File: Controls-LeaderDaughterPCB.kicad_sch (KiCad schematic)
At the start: 23 parts, among them U8 LMC555xM

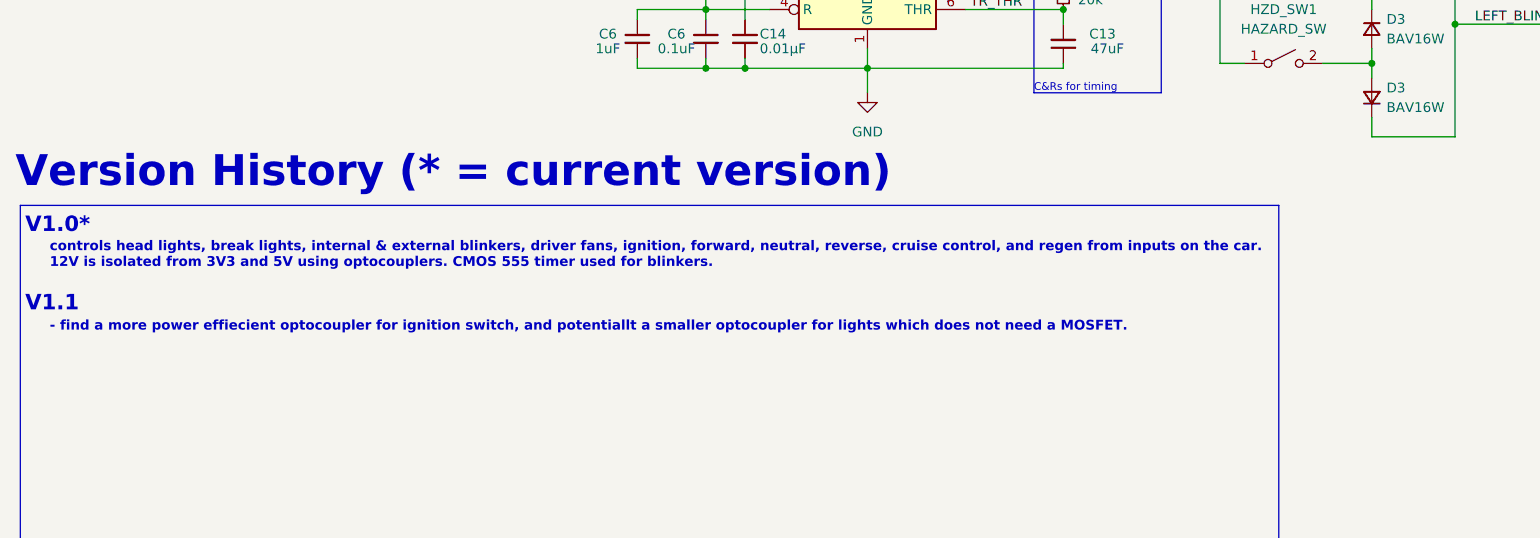
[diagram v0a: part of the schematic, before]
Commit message: lower power optocouplers now used for lights and fans, updated version history
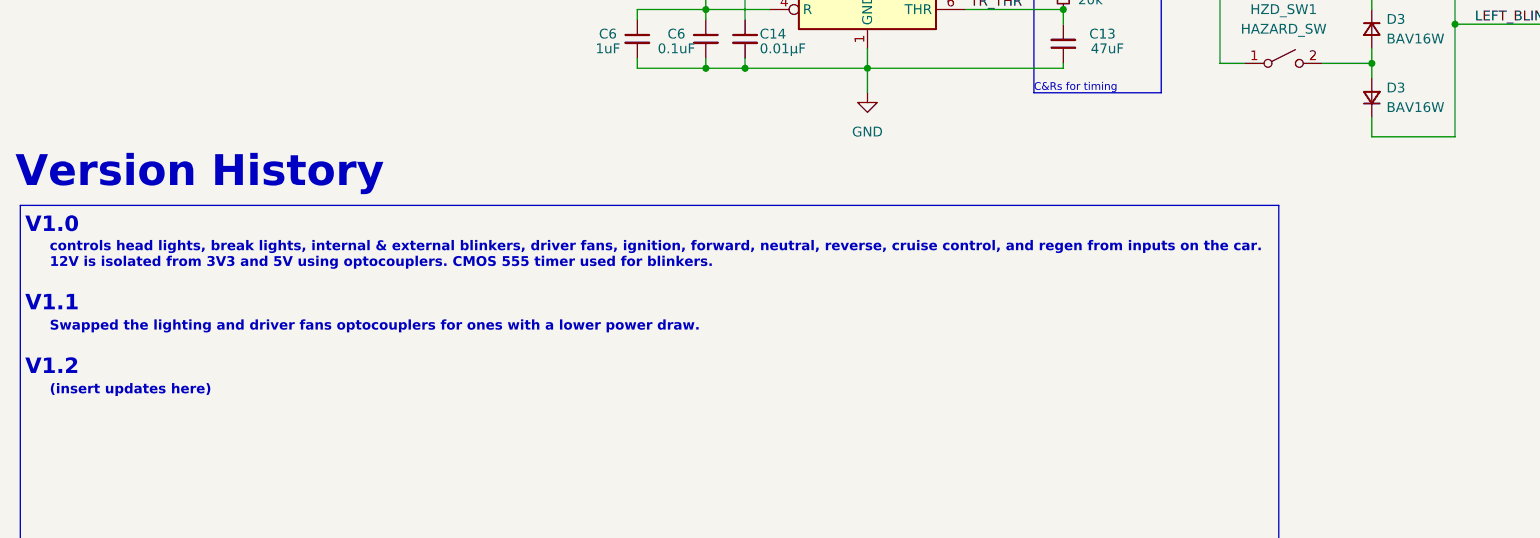
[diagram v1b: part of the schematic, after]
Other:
- note added: "(insert updates here)"
- note added: "Swapped the lighting and driver fans optocouplers for ones with a lower power draw."
- note added: "V1.0"
- note added: "V1.2"
- note added: "Version History"
- note removed: "- find a more power effiecient optocoupler for ignition switch, and potentiallt a smaller optocoupler for lights which does not need a MOSFET."
- note removed: "V1.0*"
- note removed: "Version History (* = current version)"

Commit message: changed version history
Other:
- note added: "Controls head lights, break lights, internal & external blinkers, driver fans, ignition, forward, neutral, reverse, cruise control, and regen from inputs on the car. 12V is isolated from 3V3 and 5V using optocouplers. CMOS 555 timer used for blinkers. See ReadME for more details."
- note removed: "controls head lights, break lights, internal & external blinkers, driver fans, ignition, forward, neutral, reverse, cruise control, and regen from inputs on the car. 12V is isolated from 3V3 and 5V using optocouplers. CMOS 555 timer used for blinkers."
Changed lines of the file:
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@@
     (effects (font (size 5 5) (thickness 0.7) bold) (justify left bottom))
   )
-  (text "controls head lights, break lights, internal & external blinkers, driver fans, ignition, forward, neutral, reverse, cruise control, and regen from inputs on the car.\n12V is isolated from 3V3 and 5V using optocouplers. CMOS 555 timer used for blinkers."
+  (text "Controls head lights, break lights, internal & external blinkers, driver fans, ignition, forward, neutral, reverse, cruise control, and regen from inputs on the car.\n12V is isolated from 3V3 and 5V using optocouplers. CMOS 555 timer used for blinkers. See ReadME for more details."
     (at 16.51 137.16 0)
     (effects (font (size 1.27 1.27) bold) (justify left bottom))

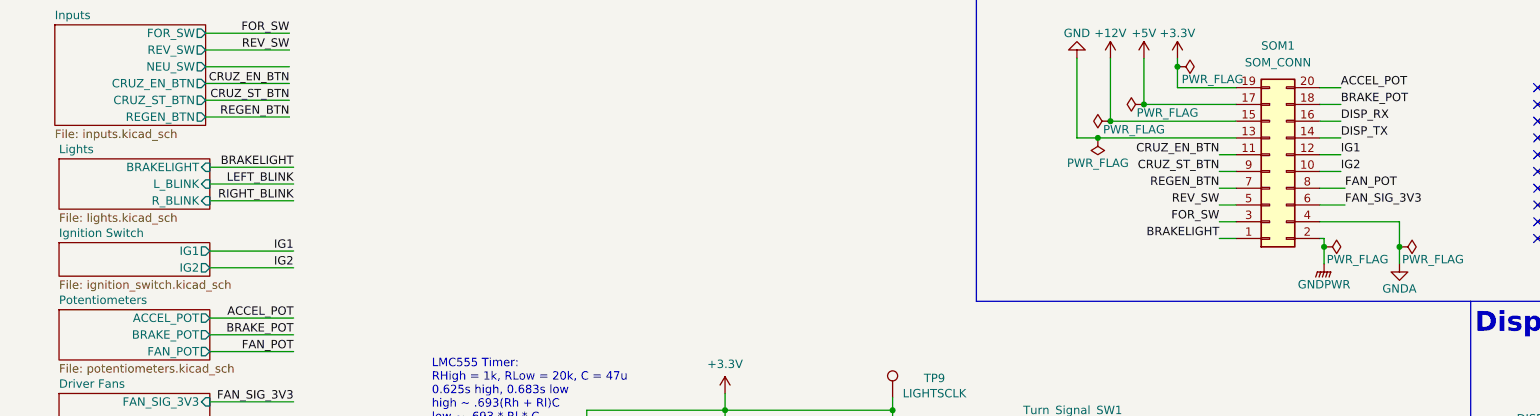
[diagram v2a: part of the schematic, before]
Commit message: Removed ignition switch connection and redid ignition signals
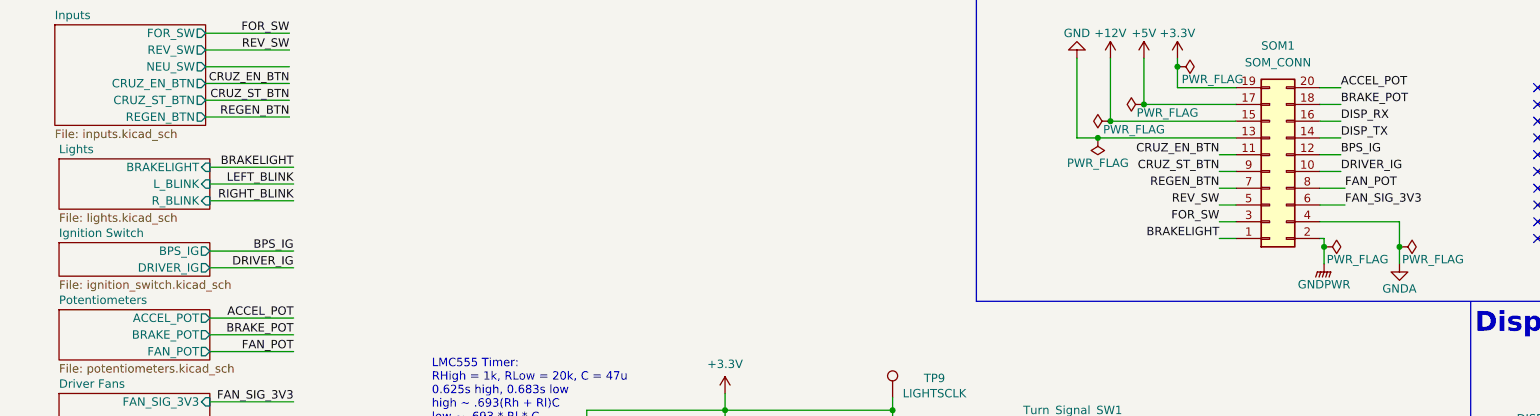
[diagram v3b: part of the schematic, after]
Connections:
- net IG1 renamed BPS_IG
- net IG2 renamed DRIVER_IG
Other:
- sheet Ignition Switch ports: added BPS_IG, DRIVER_IG; removed IG1, IG2
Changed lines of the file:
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@@
     (effects (font (size 1.27 1.27)) (justify right bottom))
   )
-  (label "IG2" (at 57.15 60.96 180) (fields_autoplaced)
+  (label "DRIVER_IG" (at 57.15 60.96 180) (fields_autoplaced)
     (effects (font (size 1.27 1.27)) (justify right bottom))
   )
@@
     (effects (font (size 1.27 1.27)) (justify right bottom))
   )
-  (label "IG2" (at 215.9 46.355 0) (fields_autoplaced)
+  (label "DRIVER_IG" (at 215.9 46.355 0) (fields_autoplaced)
     (effects (font (size 1.27 1.27)) (justify left bottom))
   )
@@
     (effects (font (size 1.27 1.27)) (justify right bottom))
   )
-  (label "IG1" (at 215.9 43.815 0) (fields_autoplaced)
+  (label "BPS_IG" (at 215.9 43.815 0) (fields_autoplaced)
     (effects (font (size 1.27 1.27)) (justify left bottom))
   )
-  (label "IG1" (at 57.15 58.42 180) (fields_autoplaced)
+  (label "BPS_IG" (at 57.15 58.42 180) (fields_autoplaced)
     (effects (font (size 1.27 1.27)) (justify right bottom))
   )
@@
       (effects (font (size 1.27 1.27)) (justify left top))
     )
-    (pin "IG1" output (at 44.45 58.42 0)
+    (pin "BPS_IG" output (at 44.45 58.42 0)
       (effects (font (size 1.27 1.27)) (justify right))
     )
-    (pin "IG2" output (at 44.45 60.96 0)
+    (pin "DRIVER_IG" output (at 44.45 60.96 0)
       (effects (font (size 1.27 1.27)) (justify right))
     )

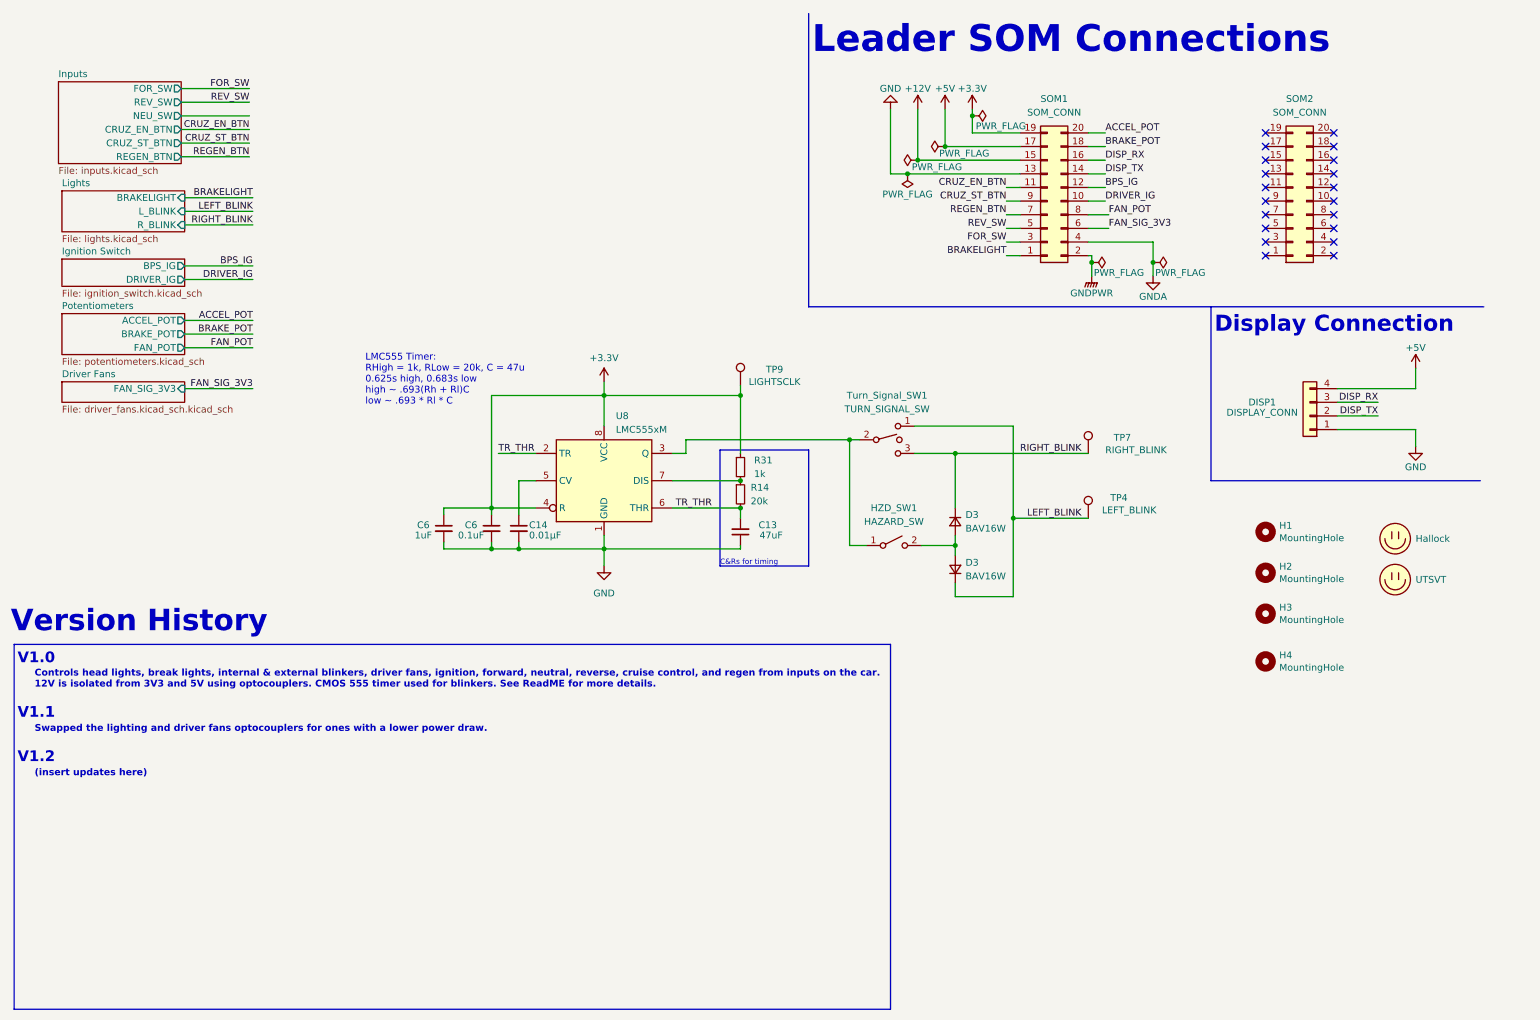
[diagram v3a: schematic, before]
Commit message: updated footprints and part numbers, added motor CAN 12V connection
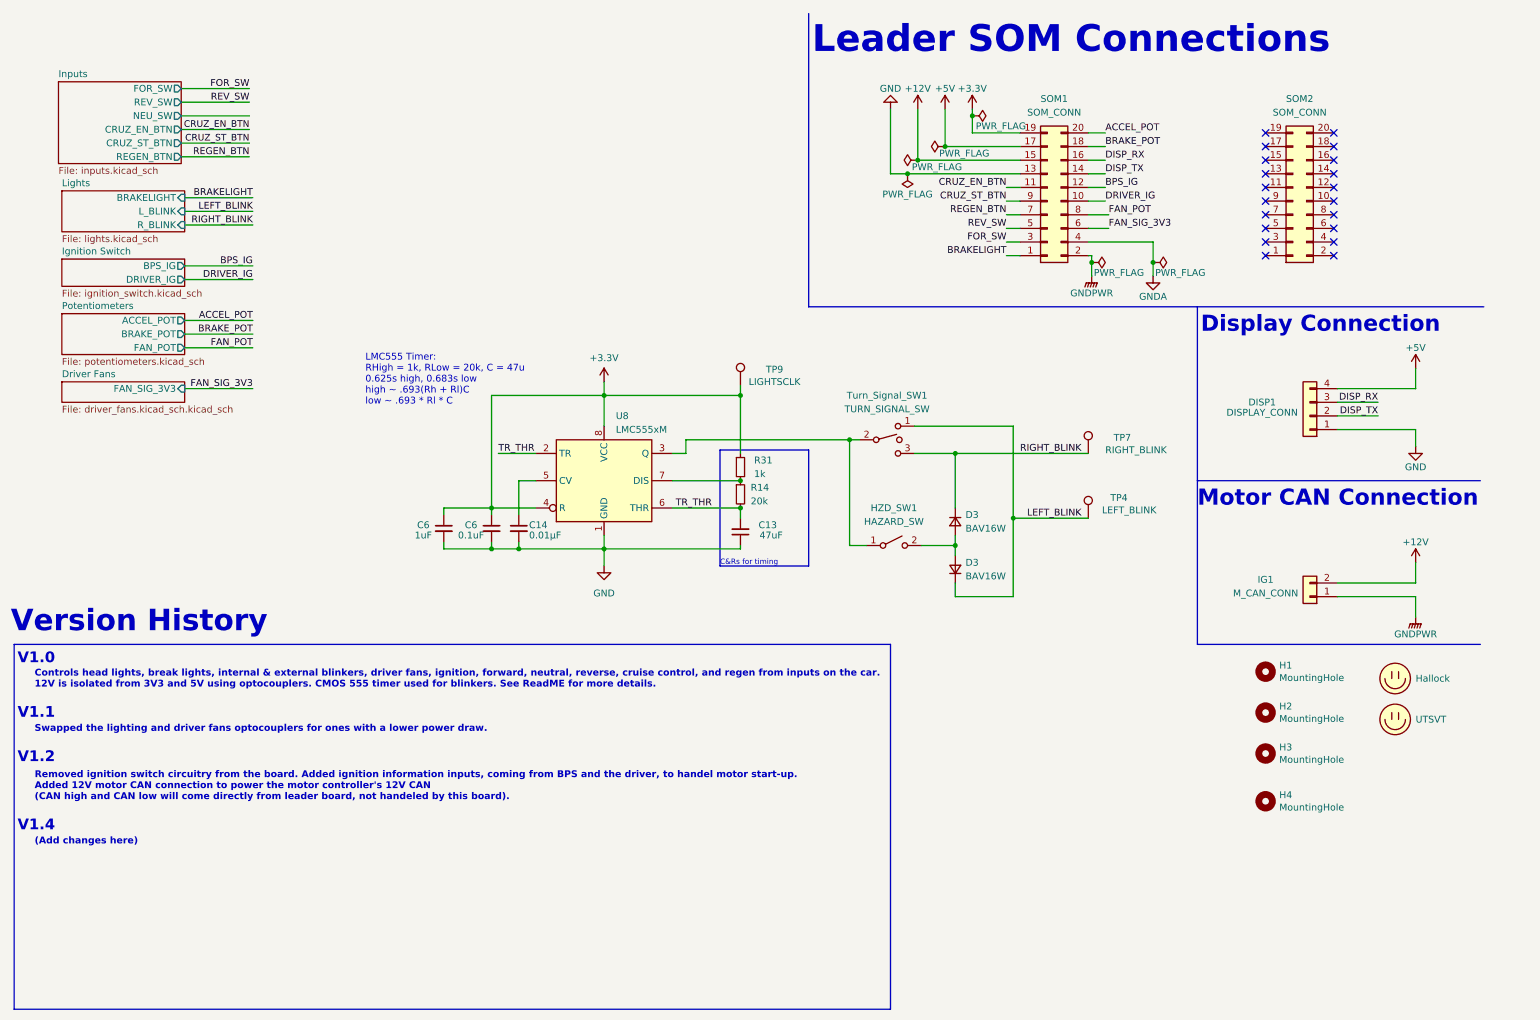
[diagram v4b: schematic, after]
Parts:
- added IG1: M_CAN_CONN, Connector_Molex:Molex_Micro-Fit_3.0_43650-0215_1x02_P3.00mm_Vertical, symbol Connector_Generic:Conn_01x02
- C13: Mauser PN (none) -> 81-GRM21BR61A476ME5L; Mouser Part Number 81-GRM21BR61A476ME5L -> (none); P/N GRM21BR61A476ME15L -> (none); PN (none) -> GRM21BR61A476ME15L
- C14: Mauser PN (none) -> 80-C0805C103J5R; Mouser Part Number 80-C0805C103J5R -> (none); P/N C0805C103J5RACTU -> (none); PN (none) -> C0805C103J5RACTU
- C6: Mauser PN (none) -> 80-C0805C105K5P; Mouser Part Number 80-C0805C105K5P -> (none); P/N C0805C105K5PACTU -> (none); PN (none) -> C0805C105K5PACTU
- C6: Mauser PN (none) -> 80-C0805C104K3R; Mouser Part Number 80-C0805C104M5R -> (none); P/N C0805C104M5RACTU -> (none); PN (none) -> C0805C104K3RACTU
- D3: Mauser PN (none) -> 621-BAV16W-F
- DISP1: Mauser PN (none) -> 538-43650-0415; Mouser Part Number 538-43650-0415 -> (none); P/N 43650-0415 -> (none); PN (none) -> 43650-0415
- HZD_SW1: P/N 43650-0215 -> (none); PN (none) -> 43650-0215
- R14: Mauser PN (none) -> 603-RP0805BRD0720KL; Mouser Part Number 603-RP0805BRD0720KL -> (none); P/N RP0805BRD0720KL -> (none); PN (none) -> RP0805BRD0720KL
- R31: Mauser PN (none) -> 71-CRCW08051K00FKEAC; Mouser Part Number 71-CRCW08051K00FKEAC -> (none); P/N CRCW08051K00FKEAC -> (none); PN (none) -> CRCW08051K00FKEAC
- SOM1, SOM2: Height 3.55 -> (none); Manufacturer_Name Molex -> (none); Manufacturer_Part_Number 52465-2070 -> (none); Mauser PN (none) -> 538-52465-2070; Mouser Part Number 538-52465-2070 -> (none); Mouser Price/Stock https://www.mouser.co.uk/ProductDetail/Molex/52465-2070?qs=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 -> (none); PN (none) -> 52465-2070
- Turn_Signal_SW1: Mauser PN (none) -> 538-43650-0315; P/N 43650-0315 -> (none); PN (none) -> 43650-0315
- U8: Mauser PN (none) -> 595-LMC555IMX/NOPB; PN (none) -> LMC555IMX/NOPB
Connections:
- net +12V: now also IG1.2 (Pin_2)
- net GNDPWR: now also IG1.1 (Pin_1)
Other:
- note added: "(Add changes here)"
- note added: "Motor CAN Connection"
- note added: "Removed ignition switch circuitry from the board. Added ignition information inputs, coming from BPS and the driver, to handel motor start-up. Added 12V motor CAN connection to power the motor controller's 12V CAN (CAN high and CAN low will come directly from leader board, not handeled by this board)."
- note added: "V1.4"
- note removed: "(insert updates here)"
- moved on the sheet: H1, H2, H3, H4

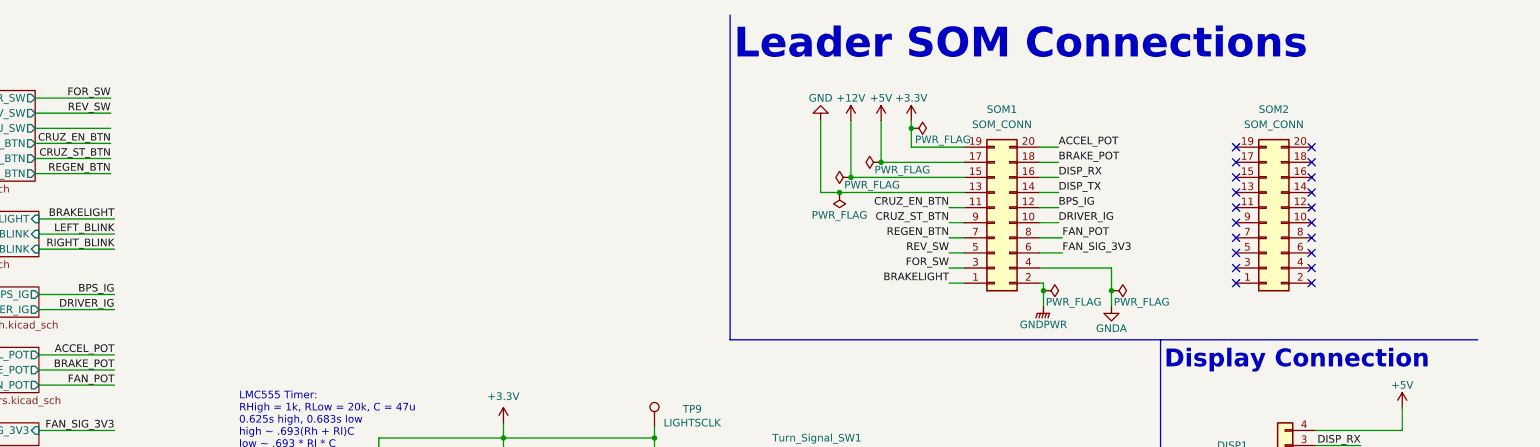
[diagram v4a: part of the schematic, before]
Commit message: Layed out SOM boot-hat connections
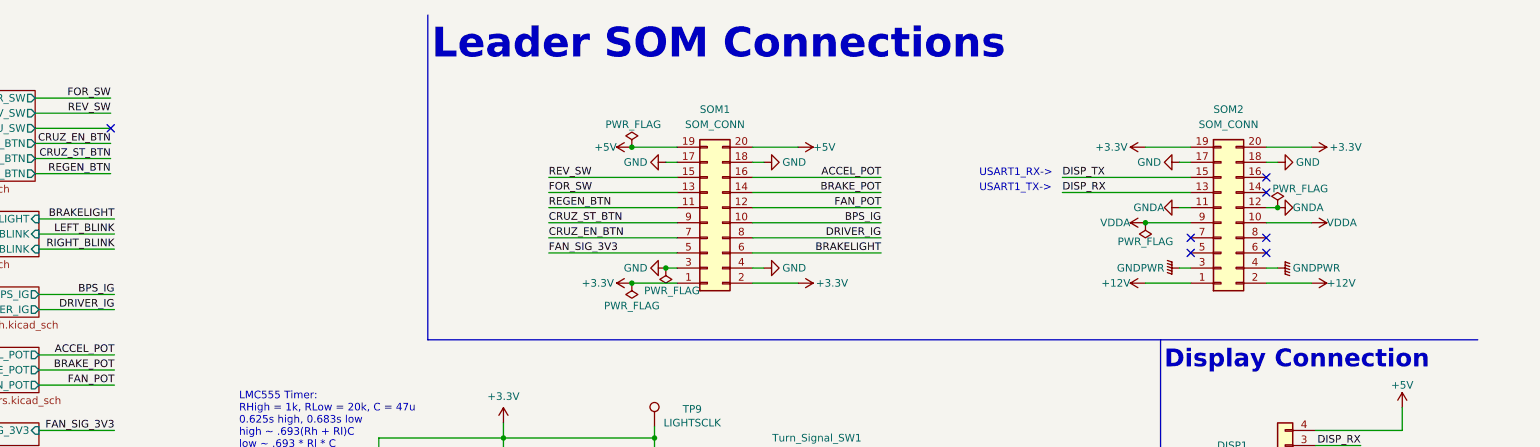
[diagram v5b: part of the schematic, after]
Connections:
- net +12V: now also SOM2.1 (Pin_1), SOM2.2 (Pin_2); no longer SOM1.15 (Pin_15)
- net +3.3V: now also SOM1.1 (Pin_1), SOM1.2 (Pin_2), SOM2.19 (Pin_19), SOM2.20 (Pin_20); no longer SOM1.19 (Pin_19)
- net +5V: now also SOM1.19 (Pin_19), SOM1.20 (Pin_20); no longer SOM1.17 (Pin_17)
- net ACCEL_POT: now also SOM1.16 (Pin_16); no longer SOM1.20 (Pin_20)
- net BPS_IG: now also SOM1.10 (Pin_10); no longer SOM1.12 (Pin_12)
- net BRAKELIGHT: now also SOM1.6 (Pin_6); no longer SOM1.1 (Pin_1)
- net BRAKE_POT: now also SOM1.14 (Pin_14); no longer SOM1.18 (Pin_18)
- net CRUZ_EN_BTN: now also SOM1.7 (Pin_7); no longer SOM1.11 (Pin_11)
- net DISP_RX: now also SOM2.13 (Pin_13); no longer SOM1.16 (Pin_16)
- net DISP_TX: now also SOM2.15 (Pin_15); no longer SOM1.14 (Pin_14)
- net DRIVER_IG: now also SOM1.8 (Pin_8); no longer SOM1.10 (Pin_10)
- net FAN_POT: now also SOM1.12 (Pin_12); no longer SOM1.8 (Pin_8)
- net FAN_SIG_3V3: now also SOM1.5 (Pin_5); no longer SOM1.6 (Pin_6)
- net FOR_SW: now also SOM1.13 (Pin_13); no longer SOM1.3 (Pin_3)
- net GND: now also SOM1.17 (Pin_17), SOM1.18 (Pin_18), SOM1.3 (Pin_3), SOM1.4 (Pin_4), SOM2.17 (Pin_17), SOM2.18 (Pin_18); no longer SOM1.13 (Pin_13)
- net GNDA: now also SOM2.11 (Pin_11), SOM2.12 (Pin_12); no longer SOM1.4 (Pin_4)
- net GNDPWR: now also SOM2.3 (Pin_3), SOM2.4 (Pin_4); no longer SOM1.2 (Pin_2)
- net REGEN_BTN: now also SOM1.11 (Pin_11); no longer SOM1.7 (Pin_7)
- net REV_SW: now also SOM1.15 (Pin_15); no longer SOM1.5 (Pin_5)
- net VDDA: now reaches SOM2.10 (Pin_10)
- net VDDA: now also SOM2.9 (Pin_9)
- no-connect marks 20 -> 7
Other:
- note added: "USART1_RX->"
- note added: "USART1_TX->"
- moved on the sheet: SOM1, SOM2
